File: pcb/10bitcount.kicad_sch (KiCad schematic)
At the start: 3 parts

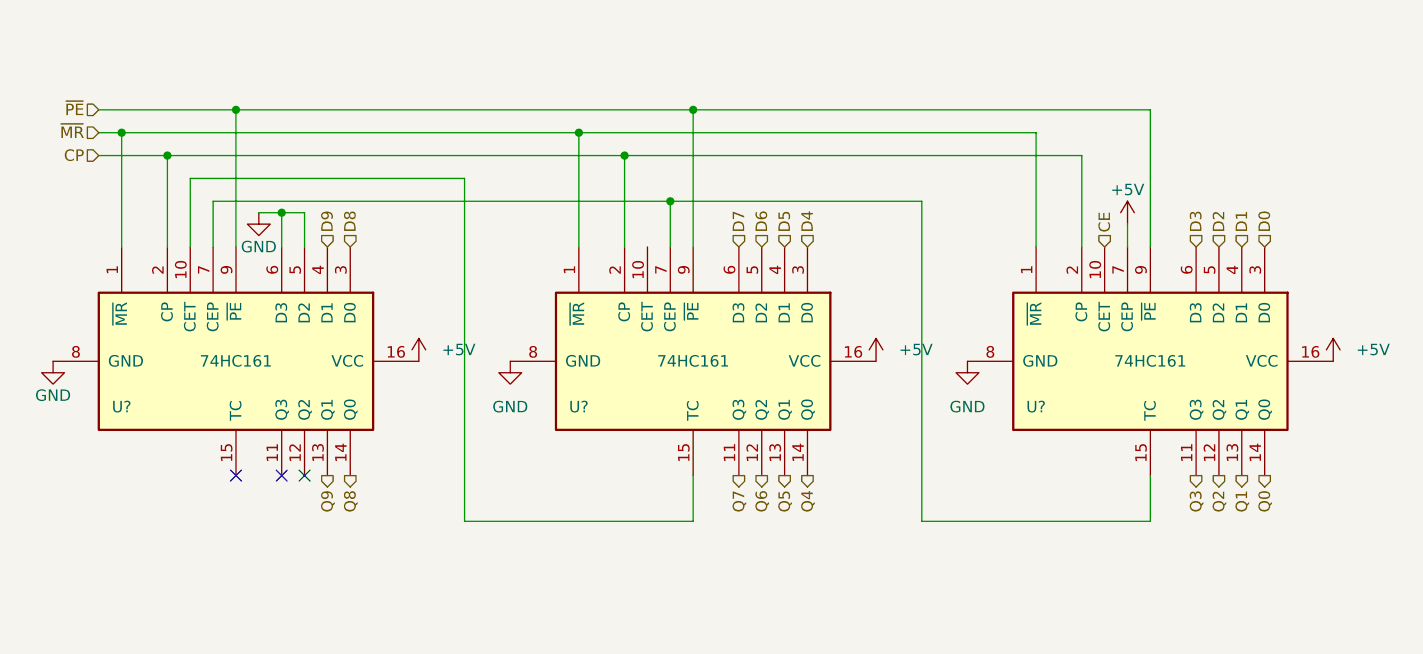
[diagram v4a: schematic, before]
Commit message: PCB: add reset circuit, xtal
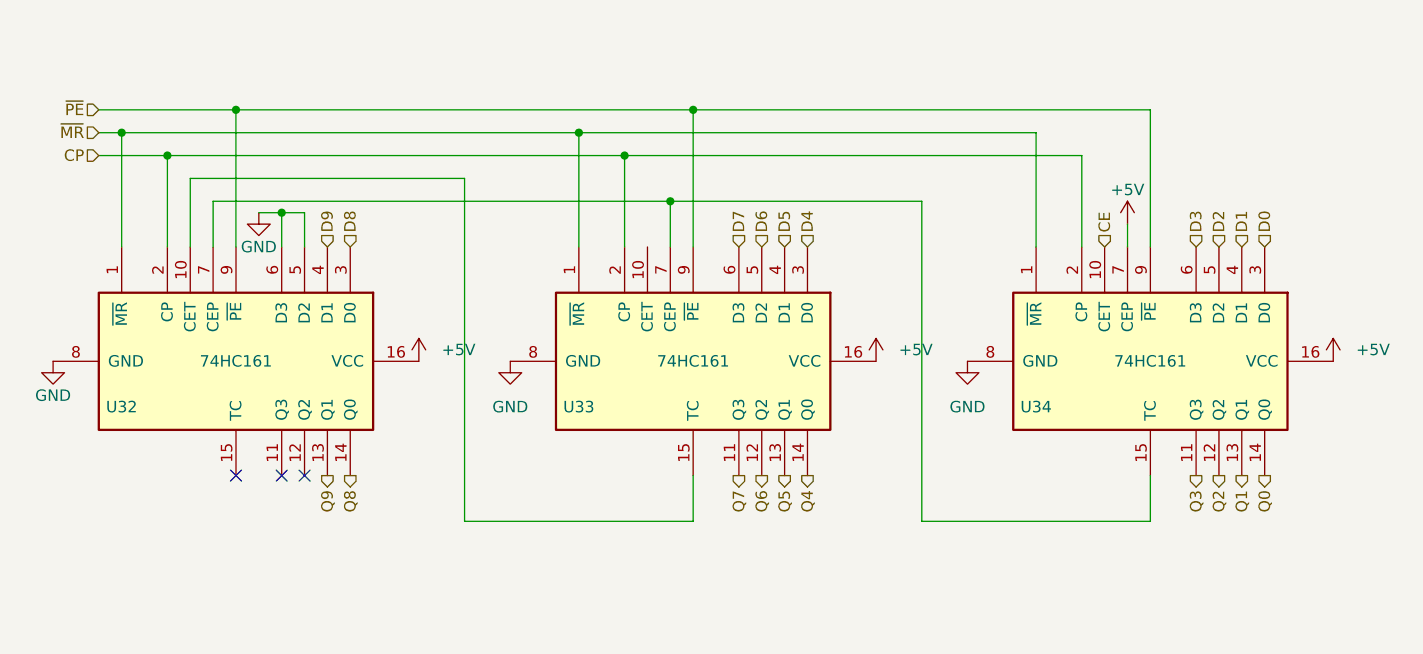
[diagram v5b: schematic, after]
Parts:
- gave numbers to parts that had none: 3
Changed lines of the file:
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@@
 (kicad_sch
-	(version 20231120)
+	(version 20250114)
 	(generator "eeschema")
-	(generator_version "8.0")
+	(generator_version "9.0")
 	(paper "A5")
 	(junction
@@
 		(dnp no)
 		(fields_autoplaced yes)
-		(property "Reference" "#PWR?"
+		(property "Reference" "#PWR0107"
 			(at 73.66 74.93 0)
 			(effects
@@
 			(project ""
 				(path "/e63e39d7-6ac0-4ffd-8aa3-1841a4541b55/90e1f016-3c60-4383-aa8d-def9977ac47b/22fed627-5774-4fe5-8536-0466d92a967a"
-					(reference "#PWR?")
+					(reference "#PWR0107")
 					(unit 1)
 				)
 				(path "/e63e39d7-6ac0-4ffd-8aa3-1841a4541b55/90e1f016-3c60-4383-aa8d-def9977ac47b/6eee35b4-65a4-4e78-9eee-35747a769478"
-					(reference "#PWR?")
+					(reference "#PWR0115")
 					(unit 1)
 				)
@@
 		(dnp no)
 		(fields_autoplaced yes)
-		(property "Reference" "#PWR?"
+		(property "Reference" "#PWR0112"
 			(at 175.26 74.93 0)
 			(effects
@@
 			(project ""
 				(path "/e63e39d7-6ac0-4ffd-8aa3-1841a4541b55/90e1f016-3c60-4383-aa8d-def9977ac47b/22fed627-5774-4fe5-8536-0466d92a967a"
-					(reference "#PWR?")
+					(reference "#PWR0112")
 					(unit 1)
 				)
 				(path "/e63e39d7-6ac0-4ffd-8aa3-1841a4541b55/90e1f016-3c60-4383-aa8d-def9977ac47b/6eee35b4-65a4-4e78-9eee-35747a769478"
-					(reference "#PWR?")
+					(reference "#PWR0120")
 					(unit 1)
 				)
@@
 		(on_board yes)
 		(dnp no)
-		(property "Reference" "U?"
+		(property "Reference" "U34"
 			(at 142.24 76.2 90)
 			(effects
@@
 			(project "fnx51"
 				(path "/e63e39d7-6ac0-4ffd-8aa3-1841a4541b55/90e1f016-3c60-4383-aa8d-def9977ac47b/22fed627-5774-4fe5-8536-0466d92a967a"
-					(reference "U?")
+					(reference "U34")
 					(unit 1)
 				)
 				(path "/e63e39d7-6ac0-4ffd-8aa3-1841a4541b55/90e1f016-3c60-4383-aa8d-def9977ac47b/6eee35b4-65a4-4e78-9eee-35747a769478"
-					(reference "U?")
+					(reference "U37")
 					(unit 1)
 				)
@@
 		(dnp no)
 		(fields_autoplaced yes)
-		(property "Reference" "#PWR?"
+		(property "Reference" "#PWR0108"
 			(at 83.82 77.47 0)
 			(effects
@@
 			(project ""
 				(path "/e63e39d7-6ac0-4ffd-8aa3-1841a4541b55/90e1f016-3c60-4383-aa8d-def9977ac47b/22fed627-5774-4fe5-8536-0466d92a967a"
-					(reference "#PWR?")
+					(reference "#PWR0108")
 					(unit 1)
 				)
 				(path "/e63e39d7-6ac0-4ffd-8aa3-1841a4541b55/90e1f016-3c60-4383-aa8d-def9977ac47b/6eee35b4-65a4-4e78-9eee-35747a769478"
-					(reference "#PWR?")
+					(reference "#PWR0116")
 					(unit 1)
 				)
@@
 		(on_board yes)
 		(dnp no)
-		(property "Reference" "#PWR?"
+		(property "Reference" "#PWR0105"
 			(at 33.02 77.47 0)
 			(effects
@@
 			(project ""
 				(path "/e63e39d7-6ac0-4ffd-8aa3-1841a4541b55/90e1f016-3c60-4383-aa8d-def9977ac47b/22fed627-5774-4fe5-8536-0466d92a967a"
-					(reference "#PWR?")
+					(reference "#PWR0105")
 					(unit 1)
 				)
 				(path "/e63e39d7-6ac0-4ffd-8aa3-1841a4541b55/90e1f016-3c60-4383-aa8d-def9977ac47b/6eee35b4-65a4-4e78-9eee-35747a769478"
-					(reference "#PWR?")
+					(reference "#PWR0113")
 					(unit 1)
 				)
@@
 		(on_board yes)
 		(dnp no)
-		(property "Reference" "#PWR?"
+		(property "Reference" "#PWR0106"
 			(at 55.88 60.96 0)
 			(effects
@@
 			(project "fnx51"
 				(path "/e63e39d7-6ac0-4ffd-8aa3-1841a4541b55/90e1f016-3c60-4383-aa8d-def9977ac47b/22fed627-5774-4fe5-8536-0466d92a967a"
-					(reference "#PWR?")
+					(reference "#PWR0106")
 					(unit 1)
 				)
 				(path "/e63e39d7-6ac0-4ffd-8aa3-1841a4541b55/90e1f016-3c60-4383-aa8d-def9977ac47b/6eee35b4-65a4-4e78-9eee-35747a769478"
-					(reference "#PWR?")
+					(reference "#PWR0114")
 					(unit 1)
 				)
@@
 		(dnp no)
 		(fields_autoplaced yes)
-		(property "Reference" "#PWR?"
+		(property "Reference" "#PWR0110"
 			(at 134.62 77.47 0)
 			(effects
@@
 			(project ""
 				(path "/e63e39d7-6ac0-4ffd-8aa3-1841a4541b55/90e1f016-3c60-4383-aa8d-def9977ac47b/22fed627-5774-4fe5-8536-0466d92a967a"
-					(reference "#PWR?")
+					(reference "#PWR0110")
 					(unit 1)
 				)
 				(path "/e63e39d7-6ac0-4ffd-8aa3-1841a4541b55/90e1f016-3c60-4383-aa8d-def9977ac47b/6eee35b4-65a4-4e78-9eee-35747a769478"
-					(reference "#PWR?")
+					(reference "#PWR0118")
 					(unit 1)
 				)
@@
 		(on_board yes)
 		(dnp no)
-		(property "Reference" "U?"
+		(property "Reference" "U33"
 			(at 91.44 76.2 90)
 			(effects
@@
 			(project "fnx51"
 				(path "/e63e39d7-6ac0-4ffd-8aa3-1841a4541b55/90e1f016-3c60-4383-aa8d-def9977ac47b/22fed627-5774-4fe5-8536-0466d92a967a"
-					(reference "U?")
+					(reference "U33")
 					(unit 1)
 				)
 				(path "/e63e39d7-6ac0-4ffd-8aa3-1841a4541b55/90e1f016-3c60-4383-aa8d-def9977ac47b/6eee35b4-65a4-4e78-9eee-35747a769478"
-					(reference "U?")
+					(reference "U36")
 					(unit 1)
 				)
@@
 		(dnp no)
 		(fields_autoplaced yes)
-		(property "Reference" "#PWR?"
+		(property "Reference" "#PWR0109"
 			(at 124.46 74.93 0)
 			(effects
@@
 			(project ""
 				(path "/e63e39d7-6ac0-4ffd-8aa3-1841a4541b55/90e1f016-3c60-4383-aa8d-def9977ac47b/22fed627-5774-4fe5-8536-0466d92a967a"
-					(reference "#PWR?")
+					(reference "#PWR0109")
 					(unit 1)
 				)
 				(path "/e63e39d7-6ac0-4ffd-8aa3-1841a4541b55/90e1f016-3c60-4383-aa8d-def9977ac47b/6eee35b4-65a4-4e78-9eee-35747a769478"
-					(reference "#PWR?")
+					(reference "#PWR0117")
 					(unit 1)
 				)
@@
 		(on_board yes)
 		(dnp no)
-		(property "Reference" "U?"
+		(property "Reference" "U32"
 			(at 40.64 76.2 90)
 			(effects
@@
 			(project ""
 				(path "/e63e39d7-6ac0-4ffd-8aa3-1841a4541b55/90e1f016-3c60-4383-aa8d-def9977ac47b/22fed627-5774-4fe5-8536-0466d92a967a"
-					(reference "U?")
+					(reference "U32")
 					(unit 1)
 				)
 				(path "/e63e39d7-6ac0-4ffd-8aa3-1841a4541b55/90e1f016-3c60-4383-aa8d-def9977ac47b/6eee35b4-65a4-4e78-9eee-35747a769478"
-					(reference "U?")
+					(reference "U35")
 					(unit 1)
 				)
@@
 		(on_board yes)
 		(dnp no)
-		(property "Reference" "#PWR?"
+		(property "Reference" "#PWR0111"
 			(at 152.4 59.69 0)
 			(effects
@@
 			(project ""
 				(path "/e63e39d7-6ac0-4ffd-8aa3-1841a4541b55/90e1f016-3c60-4383-aa8d-def9977ac47b/22fed627-5774-4fe5-8536-0466d92a967a"
-					(reference "#PWR?")
+					(reference "#PWR0111")
 					(unit 1)
 				)
 				(path "/e63e39d7-6ac0-4ffd-8aa3-1841a4541b55/90e1f016-3c60-4383-aa8d-def9977ac47b/6eee35b4-65a4-4e78-9eee-35747a769478"
-					(reference "#PWR?")
-					(unit 1)
-				)
+					(reference "#PWR0119")
+					(unit 1)
+				)

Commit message: WIP schematic
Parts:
- renumbered U32 to U33, U33 to U34, U34 to U35
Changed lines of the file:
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@@
 		(dnp no)
 		(fields_autoplaced yes)
-		(property "Reference" "#PWR0107"
+		(property "Reference" "#PWR0122"
 			(at 73.66 74.93 0)
 			(effects
@@
 			(project ""
 				(path "/e63e39d7-6ac0-4ffd-8aa3-1841a4541b55/90e1f016-3c60-4383-aa8d-def9977ac47b/22fed627-5774-4fe5-8536-0466d92a967a"
-					(reference "#PWR0107")
-					(unit 1)
-				)
-				(path "/e63e39d7-6ac0-4ffd-8aa3-1841a4541b55/90e1f016-3c60-4383-aa8d-def9977ac47b/6eee35b4-65a4-4e78-9eee-35747a769478"
-					(reference "#PWR0115")
+					(reference "#PWR0122")
+					(unit 1)
+				)
+				(path "/e63e39d7-6ac0-4ffd-8aa3-1841a4541b55/90e1f016-3c60-4383-aa8d-def9977ac47b/6eee35b4-65a4-4e78-9eee-35747a769478"
+					(reference "#PWR0130")
 					(unit 1)
 				)
@@
 		(dnp no)
 		(fields_autoplaced yes)
-		(property "Reference" "#PWR0112"
+		(property "Reference" "#PWR0127"
 			(at 175.26 74.93 0)
 			(effects
@@
 			(project ""
 				(path "/e63e39d7-6ac0-4ffd-8aa3-1841a4541b55/90e1f016-3c60-4383-aa8d-def9977ac47b/22fed627-5774-4fe5-8536-0466d92a967a"
-					(reference "#PWR0112")
-					(unit 1)
-				)
-				(path "/e63e39d7-6ac0-4ffd-8aa3-1841a4541b55/90e1f016-3c60-4383-aa8d-def9977ac47b/6eee35b4-65a4-4e78-9eee-35747a769478"
-					(reference "#PWR0120")
+					(reference "#PWR0127")
+					(unit 1)
+				)
+				(path "/e63e39d7-6ac0-4ffd-8aa3-1841a4541b55/90e1f016-3c60-4383-aa8d-def9977ac47b/6eee35b4-65a4-4e78-9eee-35747a769478"
+					(reference "#PWR0135")
 					(unit 1)
 				)
@@
 		(on_board yes)
 		(dnp no)
-		(property "Reference" "U34"
+		(property "Reference" "U35"
 			(at 142.24 76.2 90)
 			(effects
@@
 			(project "fnx51"
 				(path "/e63e39d7-6ac0-4ffd-8aa3-1841a4541b55/90e1f016-3c60-4383-aa8d-def9977ac47b/22fed627-5774-4fe5-8536-0466d92a967a"
-					(reference "U34")
-					(unit 1)
-				)
-				(path "/e63e39d7-6ac0-4ffd-8aa3-1841a4541b55/90e1f016-3c60-4383-aa8d-def9977ac47b/6eee35b4-65a4-4e78-9eee-35747a769478"
-					(reference "U37")
+					(reference "U35")
+					(unit 1)
+				)
+				(path "/e63e39d7-6ac0-4ffd-8aa3-1841a4541b55/90e1f016-3c60-4383-aa8d-def9977ac47b/6eee35b4-65a4-4e78-9eee-35747a769478"
+					(reference "U38")
 					(unit 1)
 				)
@@
 		(dnp no)
 		(fields_autoplaced yes)
-		(property "Reference" "#PWR0108"
+		(property "Reference" "#PWR0123"
 			(at 83.82 77.47 0)
 			(effects
@@
 			(project ""
 				(path "/e63e39d7-6ac0-4ffd-8aa3-1841a4541b55/90e1f016-3c60-4383-aa8d-def9977ac47b/22fed627-5774-4fe5-8536-0466d92a967a"
-					(reference "#PWR0108")
-					(unit 1)
-				)
-				(path "/e63e39d7-6ac0-4ffd-8aa3-1841a4541b55/90e1f016-3c60-4383-aa8d-def9977ac47b/6eee35b4-65a4-4e78-9eee-35747a769478"
-					(reference "#PWR0116")
+					(reference "#PWR0123")
+					(unit 1)
+				)
+				(path "/e63e39d7-6ac0-4ffd-8aa3-1841a4541b55/90e1f016-3c60-4383-aa8d-def9977ac47b/6eee35b4-65a4-4e78-9eee-35747a769478"
+					(reference "#PWR0131")
 					(unit 1)
 				)
@@
 		(on_board yes)
 		(dnp no)
-		(property "Reference" "#PWR0105"
+		(property "Reference" "#PWR0120"
 			(at 33.02 77.47 0)
 			(effects
@@
 			(project ""
 				(path "/e63e39d7-6ac0-4ffd-8aa3-1841a4541b55/90e1f016-3c60-4383-aa8d-def9977ac47b/22fed627-5774-4fe5-8536-0466d92a967a"
-					(reference "#PWR0105")
-					(unit 1)
-				)
-				(path "/e63e39d7-6ac0-4ffd-8aa3-1841a4541b55/90e1f016-3c60-4383-aa8d-def9977ac47b/6eee35b4-65a4-4e78-9eee-35747a769478"
-					(reference "#PWR0113")
+					(reference "#PWR0120")
+					(unit 1)
+				)
+				(path "/e63e39d7-6ac0-4ffd-8aa3-1841a4541b55/90e1f016-3c60-4383-aa8d-def9977ac47b/6eee35b4-65a4-4e78-9eee-35747a769478"
+					(reference "#PWR0128")
 					(unit 1)
 				)
@@
 		(on_board yes)
 		(dnp no)
-		(property "Reference" "#PWR0106"
+		(property "Reference" "#PWR0121"
 			(at 55.88 60.96 0)
 			(effects
@@
 			(project "fnx51"
 				(path "/e63e39d7-6ac0-4ffd-8aa3-1841a4541b55/90e1f016-3c60-4383-aa8d-def9977ac47b/22fed627-5774-4fe5-8536-0466d92a967a"
-					(reference "#PWR0106")
-					(unit 1)
-				)
-				(path "/e63e39d7-6ac0-4ffd-8aa3-1841a4541b55/90e1f016-3c60-4383-aa8d-def9977ac47b/6eee35b4-65a4-4e78-9eee-35747a769478"
-					(reference "#PWR0114")
+					(reference "#PWR0121")
+					(unit 1)
+				)
+				(path "/e63e39d7-6ac0-4ffd-8aa3-1841a4541b55/90e1f016-3c60-4383-aa8d-def9977ac47b/6eee35b4-65a4-4e78-9eee-35747a769478"
+					(reference "#PWR0129")
 					(unit 1)
 				)
@@
 		(dnp no)
 		(fields_autoplaced yes)
-		(property "Reference" "#PWR0110"
+		(property "Reference" "#PWR0125"
 			(at 134.62 77.47 0)
 			(effects
@@
 			(project ""
 				(path "/e63e39d7-6ac0-4ffd-8aa3-1841a4541b55/90e1f016-3c60-4383-aa8d-def9977ac47b/22fed627-5774-4fe5-8536-0466d92a967a"
-					(reference "#PWR0110")
-					(unit 1)
-				)
-				(path "/e63e39d7-6ac0-4ffd-8aa3-1841a4541b55/90e1f016-3c60-4383-aa8d-def9977ac47b/6eee35b4-65a4-4e78-9eee-35747a769478"
-					(reference "#PWR0118")
+					(reference "#PWR0125")
+					(unit 1)
+				)
+				(path "/e63e39d7-6ac0-4ffd-8aa3-1841a4541b55/90e1f016-3c60-4383-aa8d-def9977ac47b/6eee35b4-65a4-4e78-9eee-35747a769478"
+					(reference "#PWR0133")
 					(unit 1)
 				)
@@
 		(on_board yes)
 		(dnp no)
-		(property "Reference" "U33"
+		(property "Reference" "U34"
 			(at 91.44 76.2 90)
 			(effects
@@
 			(project "fnx51"
 				(path "/e63e39d7-6ac0-4ffd-8aa3-1841a4541b55/90e1f016-3c60-4383-aa8d-def9977ac47b/22fed627-5774-4fe5-8536-0466d92a967a"
-					(reference "U33")
-					(unit 1)
-				)
-				(path "/e63e39d7-6ac0-4ffd-8aa3-1841a4541b55/90e1f016-3c60-4383-aa8d-def9977ac47b/6eee35b4-65a4-4e78-9eee-35747a769478"
-					(reference "U36")
+					(reference "U34")
+					(unit 1)
+				)
+				(path "/e63e39d7-6ac0-4ffd-8aa3-1841a4541b55/90e1f016-3c60-4383-aa8d-def9977ac47b/6eee35b4-65a4-4e78-9eee-35747a769478"
+					(reference "U37")
 					(unit 1)
 				)
@@
 		(dnp no)
 		(fields_autoplaced yes)
-		(property "Reference" "#PWR0109"
+		(property "Reference" "#PWR0124"
 			(at 124.46 74.93 0)
 			(effects
@@
 			(project ""
 				(path "/e63e39d7-6ac0-4ffd-8aa3-1841a4541b55/90e1f016-3c60-4383-aa8d-def9977ac47b/22fed627-5774-4fe5-8536-0466d92a967a"
-					(reference "#PWR0109")
-					(unit 1)
-				)
-				(path "/e63e39d7-6ac0-4ffd-8aa3-1841a4541b55/90e1f016-3c60-4383-aa8d-def9977ac47b/6eee35b4-65a4-4e78-9eee-35747a769478"
-					(reference "#PWR0117")
+					(reference "#PWR0124")
+					(unit 1)
+				)
+				(path "/e63e39d7-6ac0-4ffd-8aa3-1841a4541b55/90e1f016-3c60-4383-aa8d-def9977ac47b/6eee35b4-65a4-4e78-9eee-35747a769478"
+					(reference "#PWR0132")
 					(unit 1)
 				)
@@
 		(on_board yes)
 		(dnp no)
-		(property "Reference" "U32"
+		(property "Reference" "U33"
 			(at 40.64 76.2 90)
 			(effects
@@
 			(project ""
 				(path "/e63e39d7-6ac0-4ffd-8aa3-1841a4541b55/90e1f016-3c60-4383-aa8d-def9977ac47b/22fed627-5774-4fe5-8536-0466d92a967a"
-					(reference "U32")
-					(unit 1)
-				)
-				(path "/e63e39d7-6ac0-4ffd-8aa3-1841a4541b55/90e1f016-3c60-4383-aa8d-def9977ac47b/6eee35b4-65a4-4e78-9eee-35747a769478"
-					(reference "U35")
+					(reference "U33")
+					(unit 1)
+				)
+				(path "/e63e39d7-6ac0-4ffd-8aa3-1841a4541b55/90e1f016-3c60-4383-aa8d-def9977ac47b/6eee35b4-65a4-4e78-9eee-35747a769478"
+					(reference "U36")
 					(unit 1)
 				)
@@
 		(on_board yes)
 		(dnp no)
-		(property "Reference" "#PWR0111"
+		(property "Reference" "#PWR0126"
 			(at 152.4 59.69 0)
 			(effects
@@
 			(project ""
 				(path "/e63e39d7-6ac0-4ffd-8aa3-1841a4541b55/90e1f016-3c60-4383-aa8d-def9977ac47b/22fed627-5774-4fe5-8536-0466d92a967a"
-					(reference "#PWR0111")
-					(unit 1)
-				)
-				(path "/e63e39d7-6ac0-4ffd-8aa3-1841a4541b55/90e1f016-3c60-4383-aa8d-def9977ac47b/6eee35b4-65a4-4e78-9eee-35747a769478"
-					(reference "#PWR0119")
-					(unit 1)
-				)
+					(reference "#PWR0126")
+					(unit 1)
+				)
+				(path "/e63e39d7-6ac0-4ffd-8aa3-1841a4541b55/90e1f016-3c60-4383-aa8d-def9977ac47b/6eee35b4-65a4-4e78-9eee-35747a769478"
+					(reference "#PWR0134")
+					(unit 1)
+				)
